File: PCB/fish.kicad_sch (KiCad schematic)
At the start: 7 parts, among them J1 DE9_Socket_MountingHoles, J7 643280100305, J9 643280100305

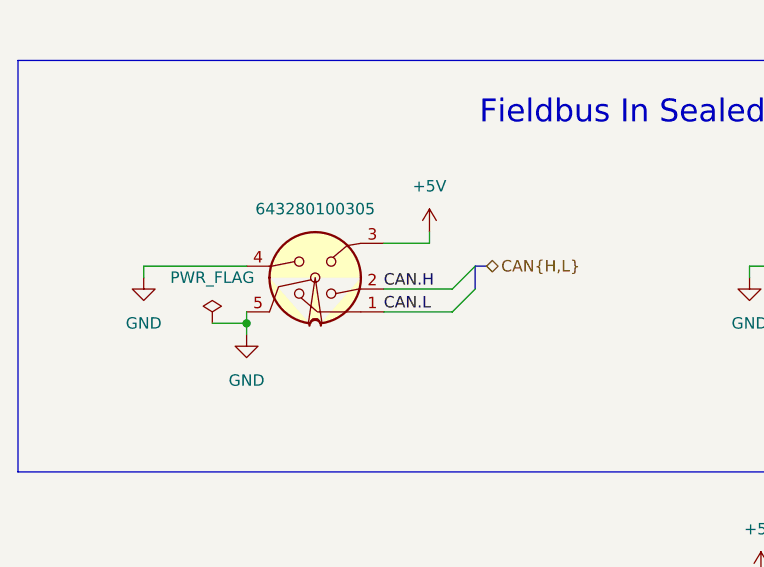
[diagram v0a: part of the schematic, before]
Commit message: placed banana connectors for power
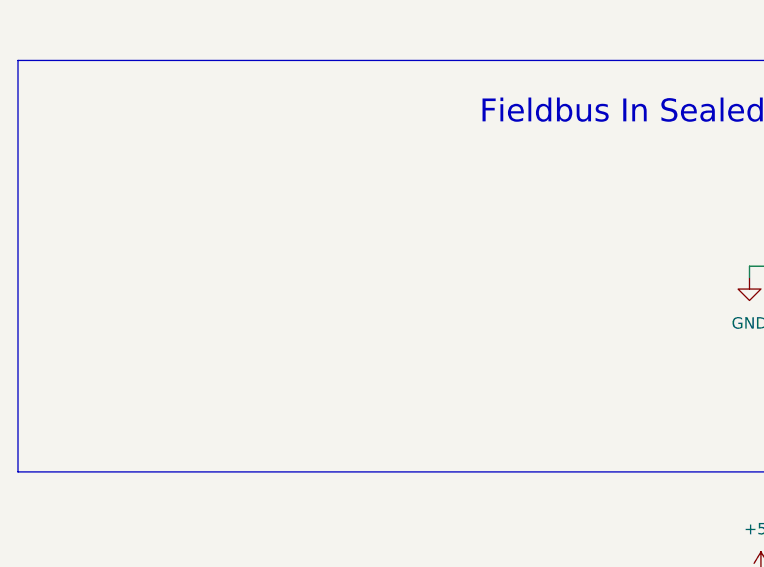
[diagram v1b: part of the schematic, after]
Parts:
- removed J7: 643280100305, dz_con:Wuerth_WR_CIRCM_643280100305, symbol #dzdb:s_con/CON-WURT-643280100305
